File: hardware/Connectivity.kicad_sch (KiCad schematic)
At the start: 17 parts, among them U6 MCP2542FD-E/MF, U7 MCP2542FD-E/MF

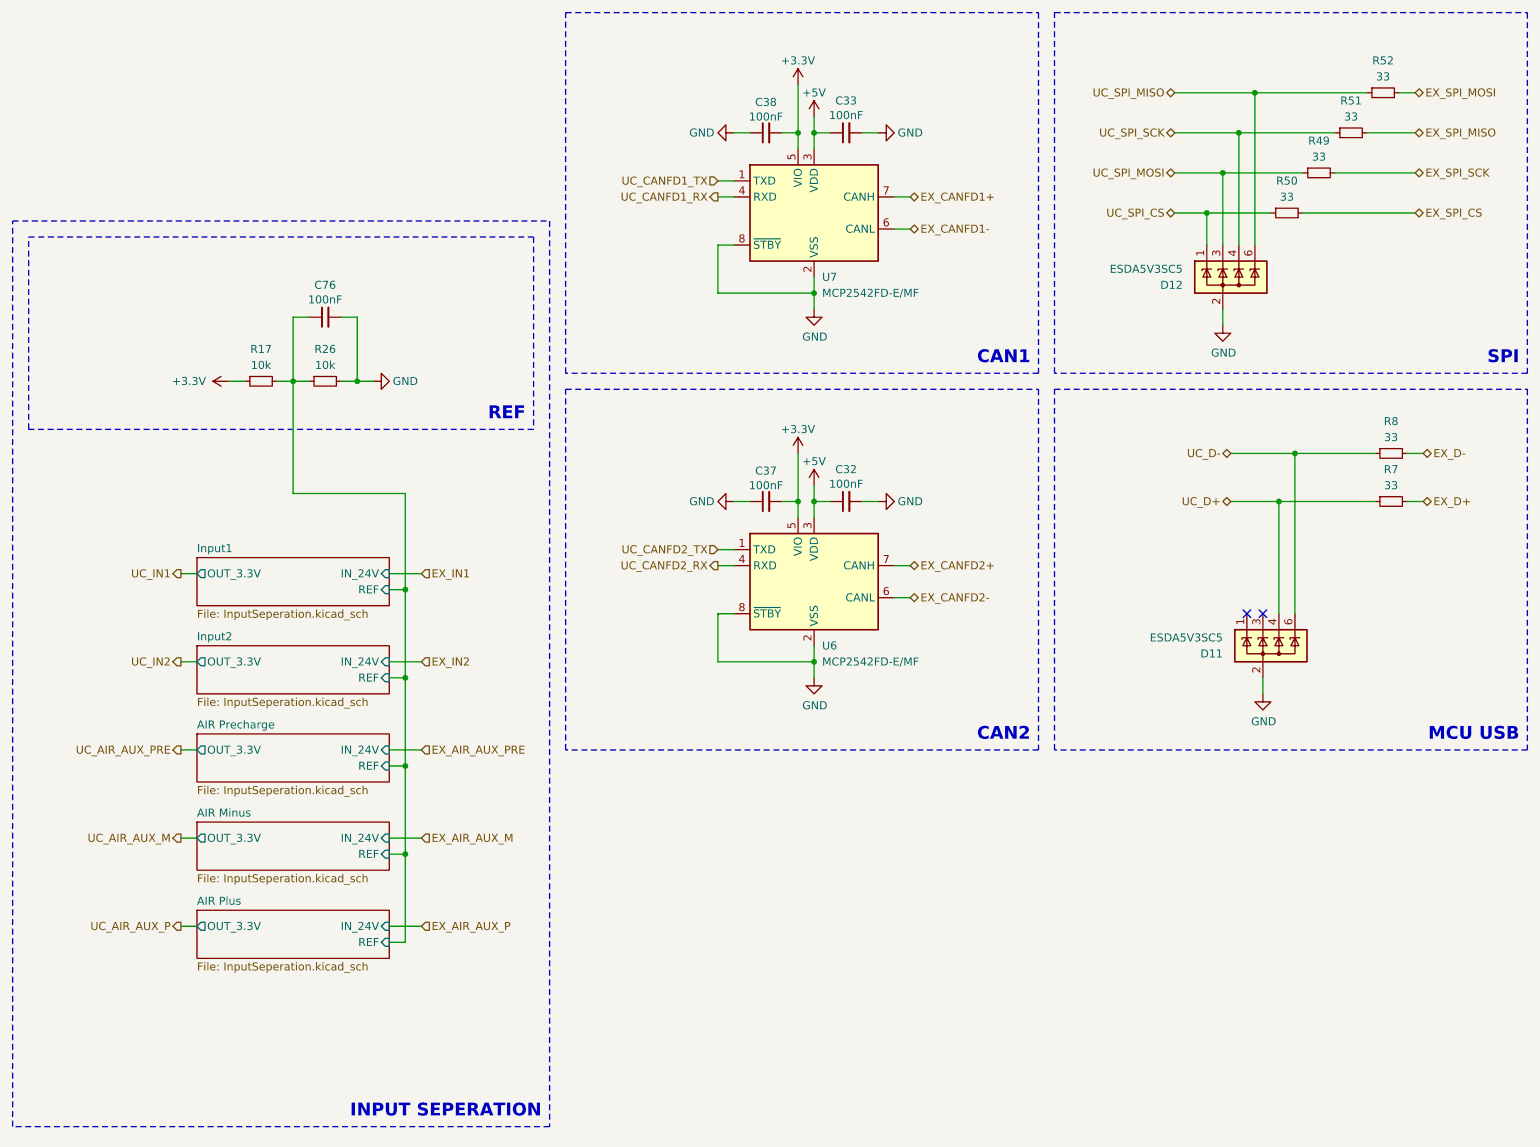
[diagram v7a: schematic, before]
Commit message: sync, layout done, now its time for the routing
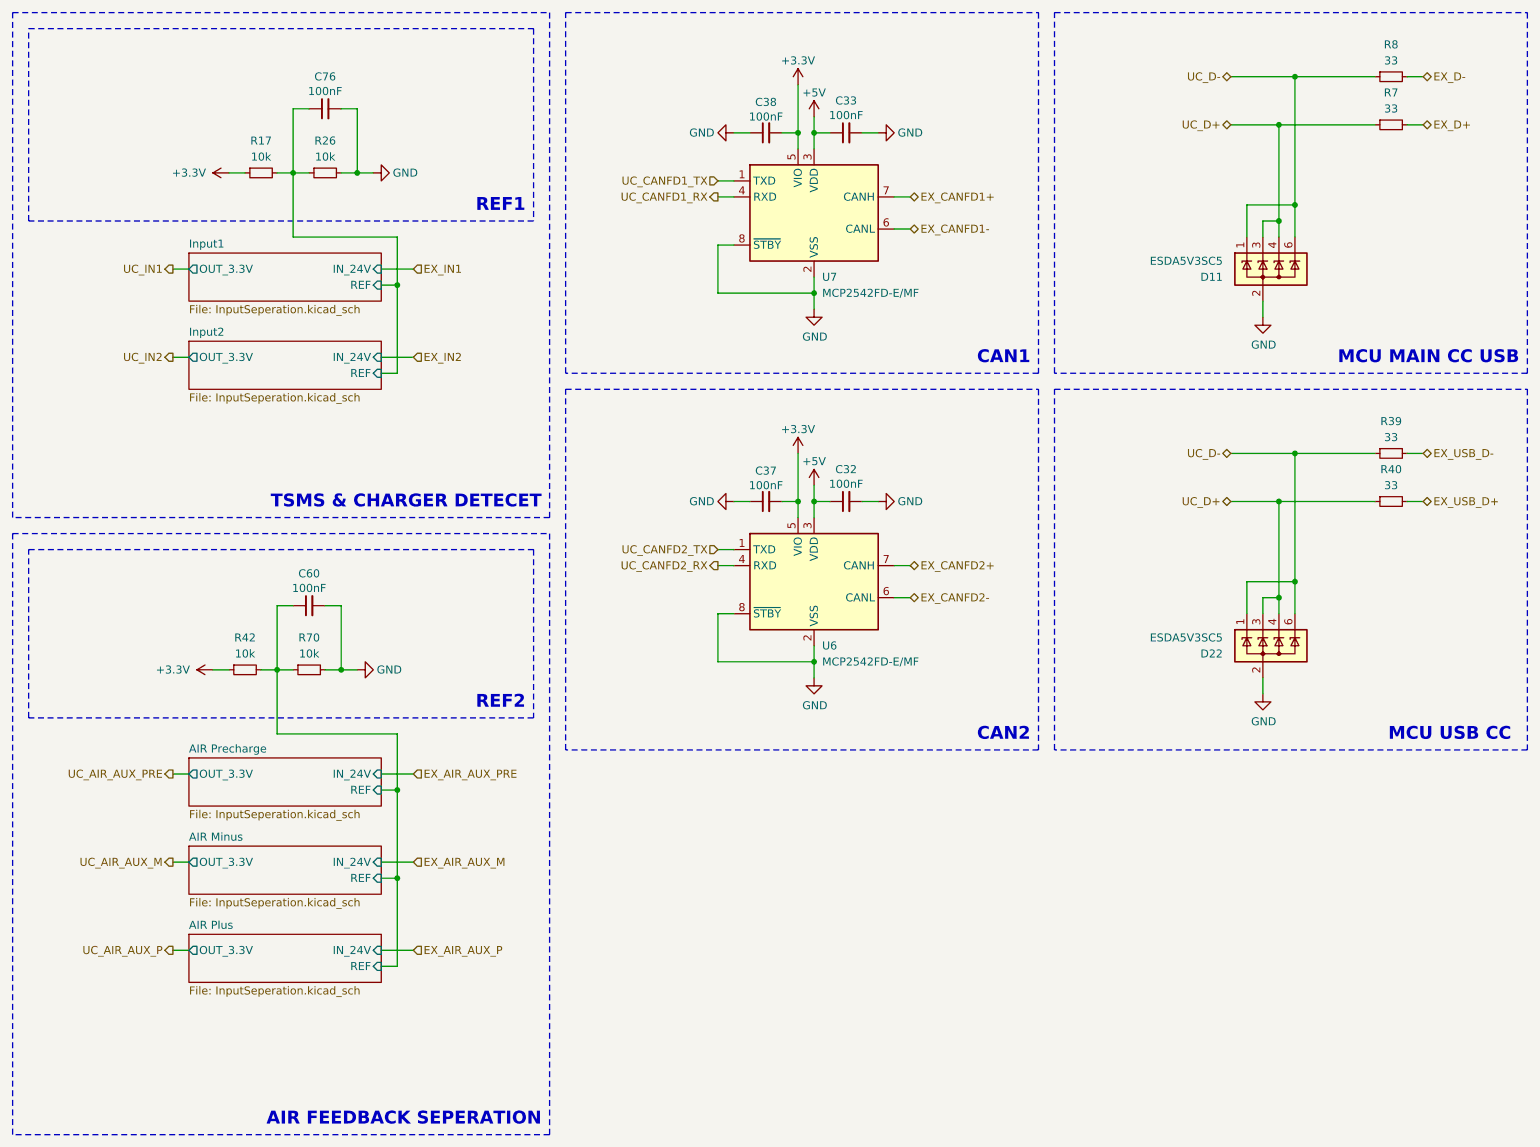
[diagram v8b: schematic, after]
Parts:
- removed D12: ESDA5V3SC5, Package_TO_SOT_SMD:SOT-23-6, symbol Power_Protection:ESDA5V3SC5
- removed R49, R50, R51, R52: 33, Resistor_SMD:R_0603_1608Metric, symbol Device:R_Small
- added C60: 100nF, Capacitor_SMD:C_0603_1608Metric, symbol Device:C_Small
- added D22: ESDA5V3SC5, Package_TO_SOT_SMD:SOT-23-6, symbol Power_Protection:ESDA5V3SC5
- added R39, R40: 33, Resistor_SMD:R_0603_1608Metric, symbol Device:R_Small
- added R42, R70: 10k, Resistor_SMD:R_0603_1608Metric, symbol Device:R_Small
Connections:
- net +3.3V: now also R42.1
- net AIR Minus/REF: now also C60.1, R42.2, R70.1; no longer C76.1, R17.2, R26.1
- net GND: now also C60.2, D22.2 (K), D22.5 (NC), R70.2
- net UC_D+: now also D11.3 (A), D22.3 (A), D22.4 (A), R40.1
- net UC_D-: now also D11.1 (A), D22.1 (A), D22.6 (A), R39.1
- new net EX_USB_D+: R40.2
- new net EX_USB_D-: R39.2
- new net Input1/REF: C76.1, R17.2, R26.1
- no-connect marks 2 -> 0
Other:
- note added: "AIR FEEDBACK SEPERATION"
- note added: "MCU MAIN CC USB"
- note added: "MCU USB CC"
- note added: "REF1"
- note added: "REF2"
- note added: "TSMS & CHARGER DETECET"
- note removed: "INPUT SEPERATION"
- note removed: "MCU USB"
- note removed: "REF"
- note removed: "SPI"
- moved on the sheet: C76, D11, R17, R26, R7, R8
